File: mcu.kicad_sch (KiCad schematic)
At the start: 55 parts, among them J3 Molex PicoBlade 2Pin, J4 Molex PicoBlade 4Pin, J5 Molex PicoBlade 2Pin, J6 6Pin DuPont 2.56mm, J7 Molex PicoBlade 2Pin, J8 Molex PicoBlade 3Pin, J9 Molex PicoBlade 2Pin, Q1 IRLML0030, SW1 SW_Reset, U3 24LC64, U4 STM32G0B1KET, U5 USBLC6-2SC6, U6 USBLC6-2SC6, Y1 ABM3B-16MHz

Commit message: Some changes to schematic
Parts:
- C7: value 100n -> 100nF
- J3: value Molex PicoBlade 2Pin -> Nerdstern
- J4: value Molex PicoBlade 4Pin -> HallEncoder
- J5: value Molex PicoBlade 2Pin -> MotorNTC
- J7: value Molex PicoBlade 2Pin -> DoorState
- J8: value Molex PicoBlade 3Pin -> OpenCloseButtons
- J9: value Molex PicoBlade 2Pin -> LockState
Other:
- note added: "with ESD protection"
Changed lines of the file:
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@@
     (stroke (width 0) (type default) (color 0 0 0 0))
   )
-  (polyline (pts (xy 63.5 13.97) (xy 100.33 13.97))
+  (polyline (pts (xy 63.5 13.97) (xy 101.6 13.97))
     (stroke (width 0) (type default) (color 0 0 0 0))
   )
@@
     (stroke (width 0) (type default) (color 0 0 0 0))
   )
-  (polyline (pts (xy 63.5 49.53) (xy 100.33 49.53))
+  (polyline (pts (xy 63.5 49.53) (xy 101.6 49.53))
     (stroke (width 0) (type default) (color 0 0 0 0))
   )
@@
     (stroke (width 0) (type default) (color 0 0 0 0))
   )
-  (polyline (pts (xy 100.33 49.53) (xy 100.33 13.97))
+  (polyline (pts (xy 101.6 49.53) (xy 101.6 13.97))
     (stroke (width 0) (type default) (color 0 0 0 0))
   )
@@
     (effects (font (size 1.27 1.27) italic) (justify right bottom))
   )
+  (text "with ESD protection" (at 36.83 157.48 0)
+    (effects (font (size 1.016 1.016) italic) (justify left bottom))
+  )
   (text "Indicator LEDs" (at 15.24 87.63 0)
     (effects (font (size 1.27 1.27) (thickness 0.254) bold italic) (justify left bottom))
@@
   (text "µC pins should be 5V tolerant" (at 143.51 191.77 0)
     (effects (font (size 1.27 1.27) italic) (justify left bottom))
+  )
+  (text "with ESD protection" (at 101.6 157.48 0)
+    (effects (font (size 1.016 1.016) italic) (justify left bottom))
   )
   (text "connectors" (at 35.56 130.81 0)
@@
     (in_bom yes) (on_board yes)
     (property "Reference" "J5" (id 0) (at 42.1132 91.9226 0))
-    (property "Value" "Molex PicoBlade 2Pin" (id 1) (at 38.1 100.33 90))
+    (property "Value" "MotorNTC" (id 1) (at 38.1 100.33 90)
+      (effects (font (size 1.27 1.27)) hide)
+    )
     (property "Footprint" "Connector_Molex:Molex_PicoBlade_53047-0210_1x02_P1.25mm_Vertical" (id 2) (at 39.37 96.52 0)
       (effects (font (size 1.27 1.27)) hide)
@@
     (in_bom yes) (on_board yes)
     (property "Reference" "C17" (id 0) (at 20.32 177.8 0))
-    (property "Value" "10uF" (id 1) (at 21.59 182.88 0))
+    (property "Value" "10uF" (id 1) (at 20.955 182.88 0))
     (property "Footprint" "Capacitor_SMD:C_1206_3216Metric" (id 2) (at 16.8148 176.53 0)
       (effects (font (size 1.27 1.27)) hide)
@@
     (in_bom yes) (on_board yes)
     (property "Reference" "J8" (id 0) (at 40.64 166.37 0))
-    (property "Value" "Molex PicoBlade 3Pin" (id 1) (at 38.1 173.99 90))
+    (property "Value" "OpenCloseButtons" (id 1) (at 38.1 173.99 90)
+      (effects (font (size 1.27 1.27)) hide)
+    )
     (property "Footprint" "Connector_Molex:Molex_PicoBlade_53047-0310_1x03_P1.25mm_Vertical" (id 2) (at 39.37 171.45 0)
       (effects (font (size 1.27 1.27)) hide)
@@
     (in_bom yes) (on_board yes)
     (property "Reference" "J9" (id 0) (at 110.49 168.91 0))
-    (property "Value" "Molex PicoBlade 2Pin" (id 1) (at 114.3 175.26 0)
-      (effects (font (size 1.016 1.016)))
+    (property "Value" "LockState" (id 1) (at 114.3 175.26 0)
+      (effects (font (size 1.016 1.016)) hide)
     )
     (property "Footprint" "Connector_Molex:Molex_PicoBlade_53047-0210_1x02_P1.25mm_Vertical" (id 2) (at 109.22 171.45 0)
@@
     (in_bom yes) (on_board yes)
     (property "Reference" "J4" (id 0) (at 22.86 26.67 0))
-    (property "Value" "Molex PicoBlade 4Pin" (id 1) (at 19.05 35.56 90))
+    (property "Value" "HallEncoder" (id 1) (at 19.05 35.56 90)
+      (effects (font (size 1.27 1.27)) hide)
+    )
     (property "Footprint" "Connector_Molex:Molex_PicoBlade_53047-0410_1x04_P1.25mm_Vertical" (id 2) (at 21.59 31.75 0)
       (effects (font (size 1.27 1.27)) hide)
@@
       (effects (font (size 1.27 1.27)) (justify left))
     )
-    (property "Value" "100n" (id 1) (at 95.25 38.1 0)
+    (property "Value" "100nF" (id 1) (at 95.25 38.1 0)
       (effects (font (size 1.27 1.27)) (justify left))
     )
@@
   (symbol (lib_id "Device:Q_NMOS_SGD") (at 246.38 38.1 0) (mirror y) (unit 1)
     (in_bom yes) (on_board yes)
-    (property "Reference" "Q1" (id 0) (at 238.76 36.83 0)
-      (effects (font (size 1.27 1.27)) (justify left))
-    )
-    (property "Value" "IRLML0030" (id 1) (at 241.3 44.45 90)
+    (property "Reference" "Q1" (id 0) (at 250.19 36.195 0)
+      (effects (font (size 1.27 1.27)) (justify left))
+    )
+    (property "Value" "IRLML0030" (id 1) (at 256.54 41.91 0)
       (effects (font (size 1.27 1.27)) (justify left))
     )
@@
     (in_bom yes) (on_board yes)
     (property "Reference" "J7" (id 0) (at 110.49 160.02 0))
-    (property "Value" "Molex PicoBlade 2Pin" (id 1) (at 114.3 166.37 0)
-      (effects (font (size 1.016 1.016)))
+    (property "Value" "DoorState" (id 1) (at 114.3 166.37 0)
+      (effects (font (size 1.016 1.016)) hide)
     )
     (property "Footprint" "Connector_Molex:Molex_PicoBlade_53047-0210_1x02_P1.25mm_Vertical" (id 2) (at 109.22 162.56 0)
@@
   (symbol (lib_id "Connector:Conn_01x02_Male") (at 220.98 21.59 0) (unit 1)
     (in_bom yes) (on_board yes)
-    (property "Reference" "J3" (id 0) (at 221.615 17.814 0))
-    (property "Value" "Molex PicoBlade 2Pin" (id 1) (at 226.06 26.67 0))
+    (property "Reference" "J3" (id 0) (at 221.615 19.685 0))
+    (property "Value" "Nerdstern" (id 1) (at 226.06 26.67 0)
+      (effects (font (size 1.27 1.27)) hide)
+    )
     (property "Footprint" "Connector_Molex:Molex_PicoBlade_53047-0210_1x02_P1.25mm_Vertical" (id 2) (at 220.98 21.59 0)
       (effects (font (size 1.27 1.27)) hide)

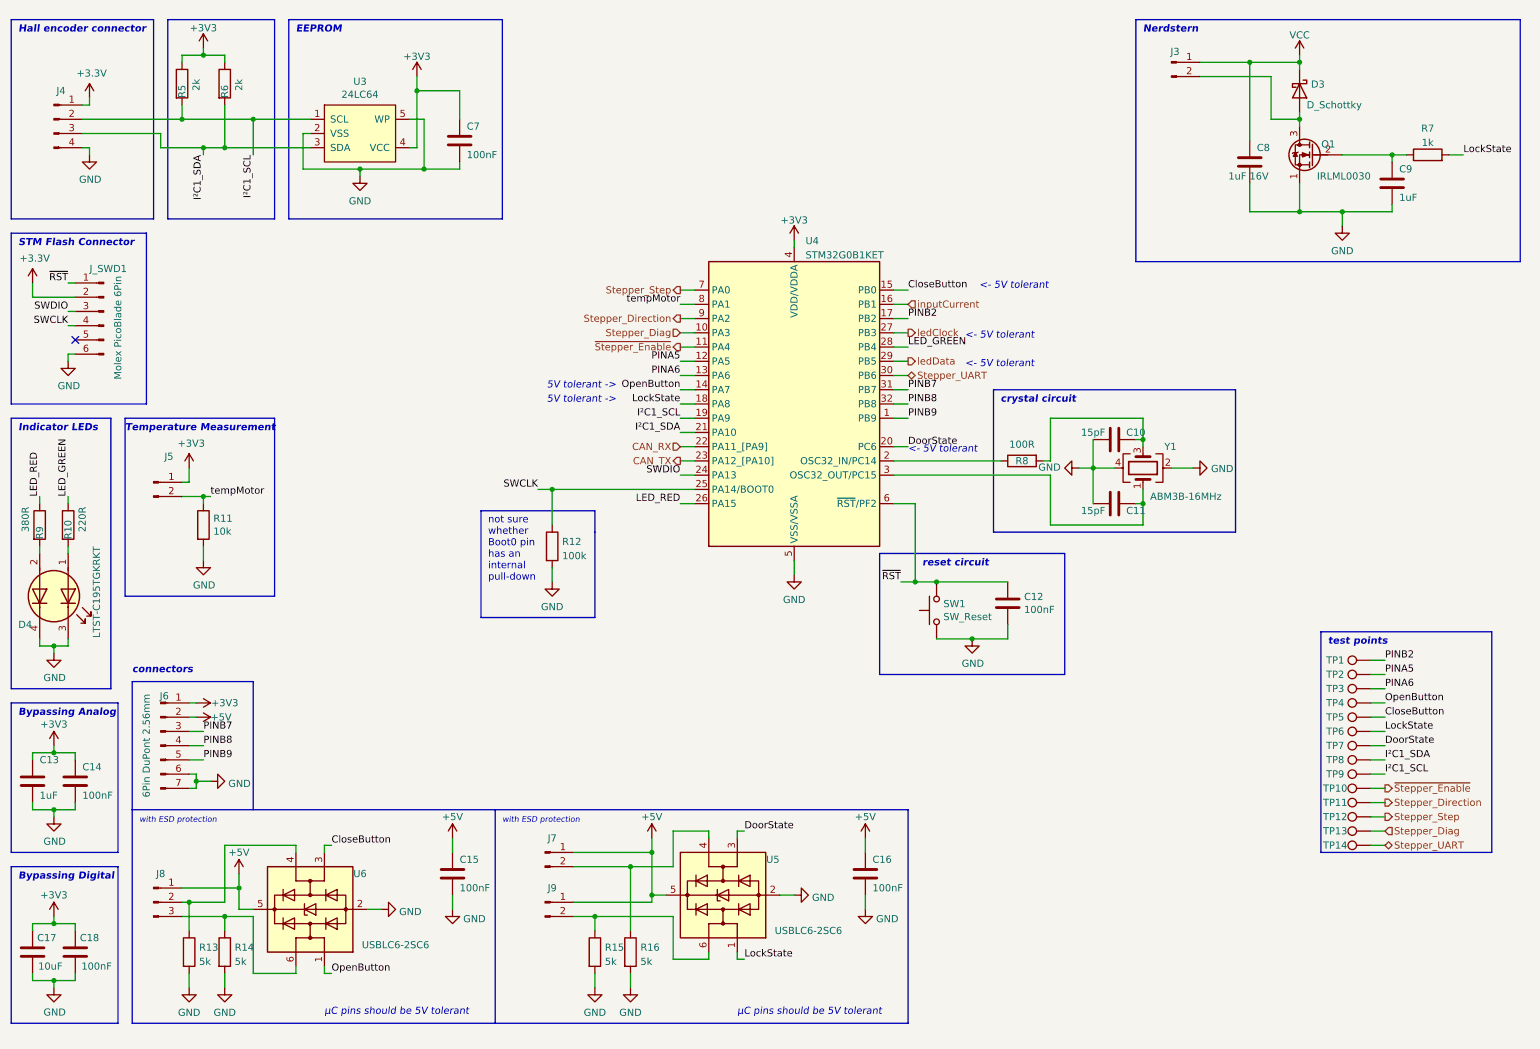
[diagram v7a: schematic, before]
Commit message: Finish PCB layout
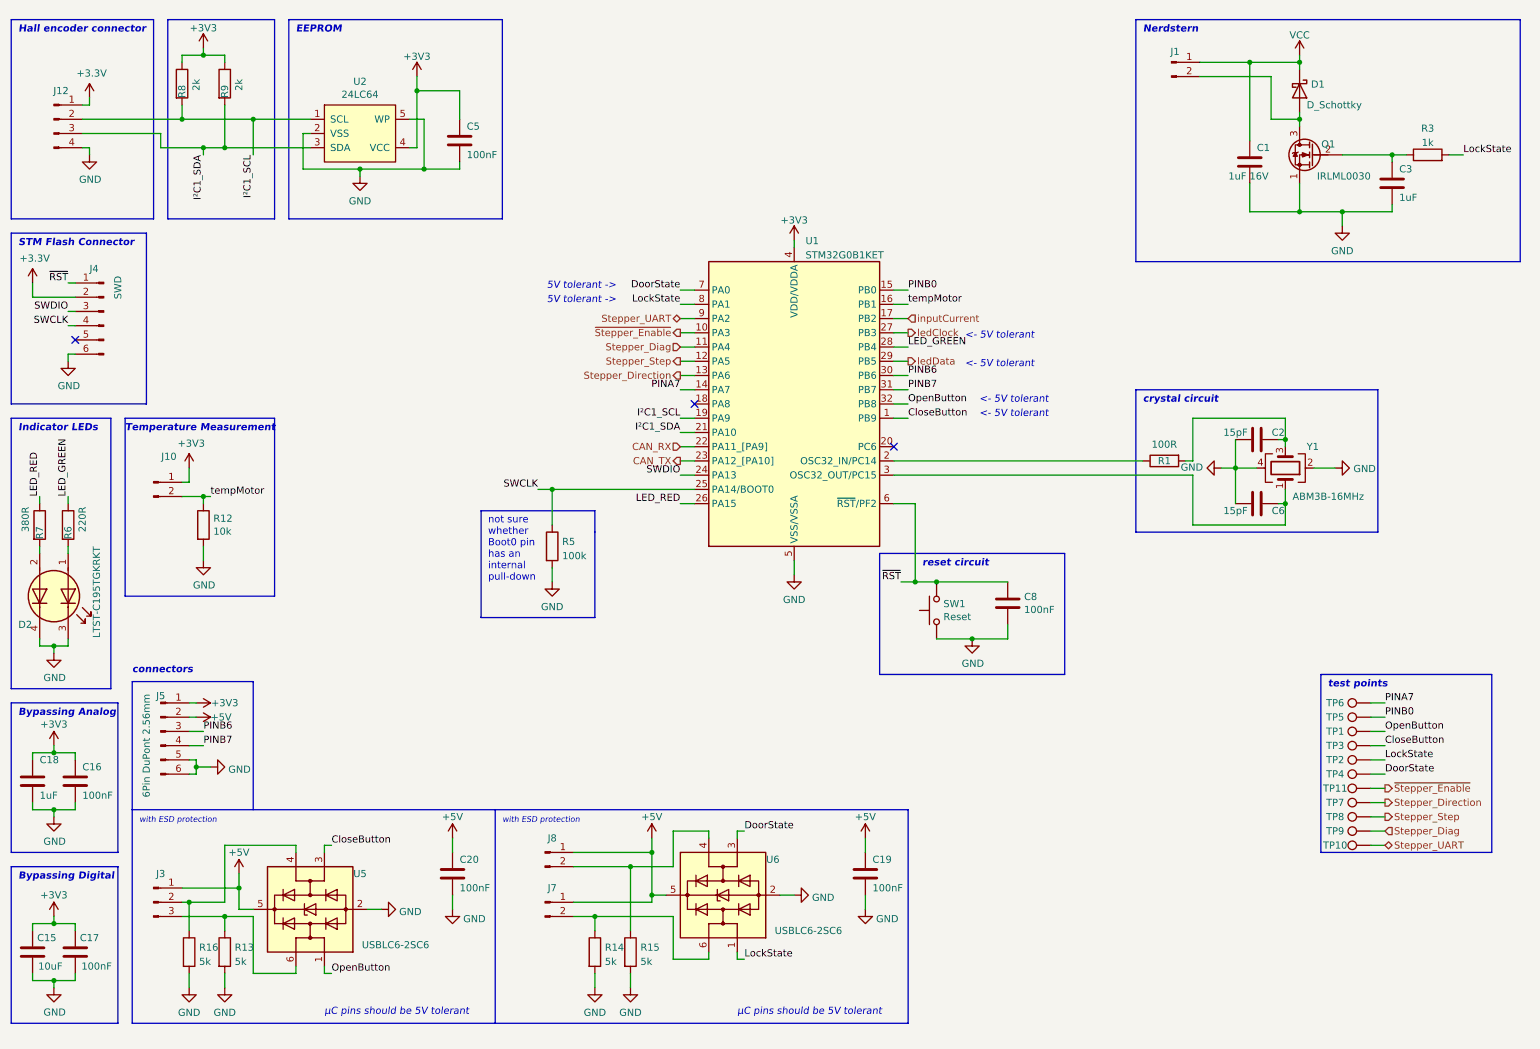
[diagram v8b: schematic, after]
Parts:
- removed TP2, TP3, TP8, TP9: TestPoint, TestPoint:TestPoint_Pad_D2.0mm, symbol Connector:TestPoint
- added TP5: TestPoint, TestPoint:TestPoint_Pad_D2.0mm, symbol Connector:TestPoint
- J3: renamed from J8; value OpenCloseButtons -> Open+Close
- J4: renamed from J_SWD1; value Molex PicoBlade 6Pin -> SWD
- J5: renamed from J6; footprint Connector_PinHeader_2.54mm:PinHeader_1x07_P2.54mm_Vertical -> Connector_PinHeader_2.54mm:PinHeader_1x06_P2.54mm_Vertical; symbol Connector:Conn_01x07_Male -> Connector:Conn_01x06_Male
- SW1: value SW_Reset -> Reset
- renumbered C8 to C1, C17 to C15, C14 to C16, C18 to C17, C13 to C18, C16 to C19, C10 to C2, C15 to C20, C9 to C3, C7 to C5, C11 to C6, C12 to C8, D3 to D1, D4 to D2, J3 to J1, J5 to J10, J4 to J12, J9 to J7, J7 to J8, R8 to R1, R11 to R12, R14 to R13, R15 to R14, R16 to R15, R13 to R16, R7 to R3, R12 to R5, R10 to R6, R9 to R7, R5 to R8, R6 to R9, TP4 to TP1, TP14 to TP10, TP10 to TP11, TP6 to TP2, TP5 to TP3, TP7 to TP4, TP1 to TP6, TP11 to TP7, TP12 to TP8, TP13 to TP9, U4 to U1, U3 to U2, U6 to U5, U5 to U6
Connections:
- net PINA5 is gone; now on net Stepper_Step: U1.12 (PA5)
- net PINA6 is gone; now on net Stepper_Direction: U1.13 (PA6)
- net CloseButton: now also U1.1 (PB9); no longer U1.15 (PB0)
- net DoorState: now also U1.7 (PA0); no longer U1.20 (PC6)
- net GND: now also J5.5 (Pin_5); no longer J5.7 (Pin_7)
- net LockState: now also U1.8 (PA1); no longer U1.18 (PA8)
- net OpenButton: now also U1.32 (PB8); no longer U1.14 (PA7)
- net PINB7: now also J5.4 (Pin_4); no longer J5.3 (Pin_3)
- net Stepper_Diag: now also U1.11 (PA4); no longer U1.10 (PA3)
- net Stepper_Direction: no longer U1.9 (PA2)
- net Stepper_Step: no longer U1.7 (PA0)
- net Stepper_UART: now also U1.9 (PA2); no longer U1.30 (PB6)
- net inputCurrent: now also U1.17 (PB2); no longer U1.16 (PB1)
- net tempMotor: now also U1.16 (PB1); no longer U1.8 (PA1)
- net ~{Stepper_Enable}: now also U1.10 (PA3); no longer U1.11 (PA4)
- net PINB2 renamed PINA7
- net PINA7: now also U1.14 (PA7); no longer U1.17 (PB2)
- removed net PINB8: J5.4 (Pin_4), U1.32 (PB8)
- removed net PINB9: J5.5 (Pin_5), U1.1 (PB9)
- new net PINB0: TP5.1, U1.15 (PB0)
- new net PINB6: J5.3 (Pin_3), U1.30 (PB6)
- no-connect marks 1 -> 3
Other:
- moved on the sheet: C2, C6, R1, TP1, TP2, TP3, TP4, TP6, Y1
